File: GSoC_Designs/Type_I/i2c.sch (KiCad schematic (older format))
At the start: 3 parts, among them U5 24AA014, U6 TCA9617A, U7 TCA9617A

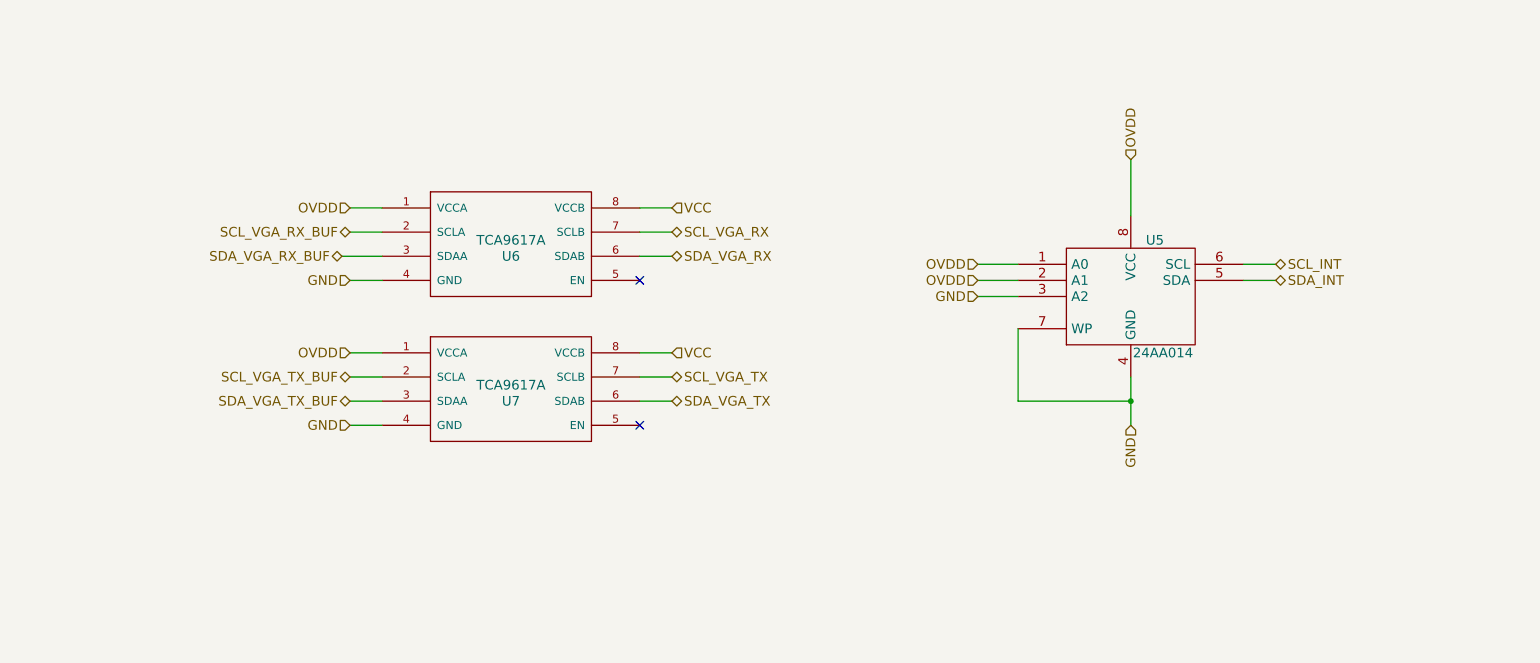
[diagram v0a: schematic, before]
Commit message: Added header for unused Pins
Unused pins are OE_Field, COAST, CLAMP and PWRDWN
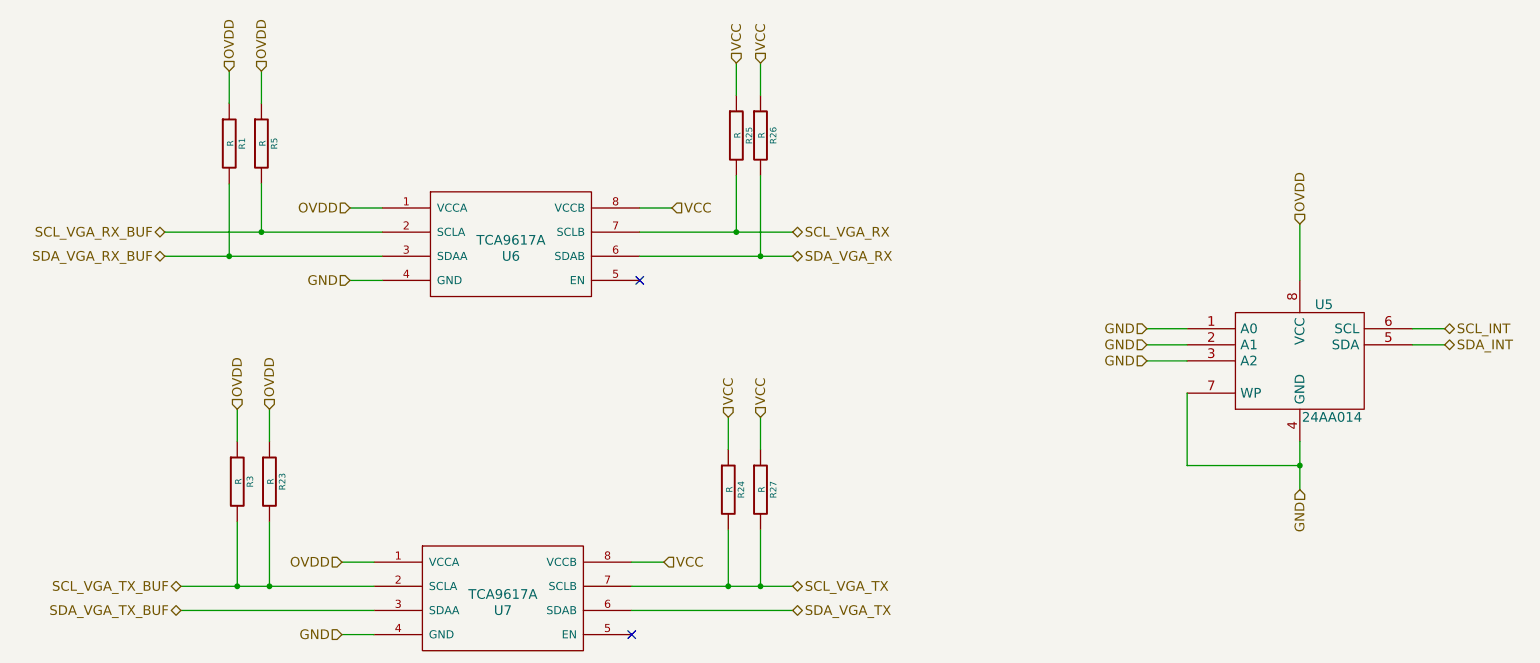
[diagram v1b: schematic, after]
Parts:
- added R1, R23, R24, R25, R26, R27, R3, R5: R, ~, symbol R
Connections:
- net GND: now also U5.1 (A0), U5.2 (A1)
- net OVDD: now also R1.1, R23.1, R3.1, R5.1; no longer U5.1 (A0), U5.2 (A1)
- net SCL_VGA_RX: now also R25.2
- net SCL_VGA_RX_BUF: now also R5.2
- net SCL_VGA_TX: now also R24.2, R27.2
- net SCL_VGA_TX_BUF: now also R23.2, R3.2
- net SDA_VGA_RX: now also R26.2
- net SDA_VGA_RX_BUF: now also R1.2
- net VCC: now also R24.1, R25.1, R26.1, R27.1
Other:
- moved on the sheet: U5, U7

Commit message: PCB Routing
70% tracks routed. Fine tuning remaining
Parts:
- R1, R23, R3, R5: value R -> 2.2K
- R24, R25, R26, R27: value R -> 4.7K
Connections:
- net SCL_VGA_TX: no longer R27.2
- net SCL_VGA_TX_BUF: no longer R3.2
- net SDA_VGA_TX: now also R27.2
- net SDA_VGA_TX_BUF: now also R3.2
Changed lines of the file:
@@
 Sheet 3 3
 Title ""
-Date "17 jul 2014"
+Date "21 jul 2014"
 Rev ""
 Comp ""
@@
 Text HLabel 10000 4150 2    60   BiDi ~ 0
 SDA_INT
-Text HLabel 5150 5500 2    60   Input ~ 0
+Text HLabel 5050 5500 2    60   Input ~ 0
 VCC
 Text HLabel 9100 3400 1    60   Input ~ 0
@@
 	1    0    0    -1
 $EndComp
-Text HLabel 3200 3300 0    60   Input ~ 0
-OVDD
-Text HLabel 3150 5500 0    60   Input ~ 0
-OVDD
-Text HLabel 3150 5950 0    60   Input ~ 0
-GND
-Text HLabel 3200 3750 0    60   Input ~ 0
+Text HLabel 3300 3300 0    60   Input ~ 0
+OVDD
+Text HLabel 3250 5500 0    60   Input ~ 0
+OVDD
+Text HLabel 3250 5950 0    60   Input ~ 0
+GND
+Text HLabel 3300 3750 0    60   Input ~ 0
 GND
 NoConn ~ 4950 5950
 NoConn ~ 5000 3750
-Wire Wire Line
-	9800 4050 10000 4050
-Wire Wire Line
-	9800 4150 10000 4150
-Wire Wire Line
-	9100 3400 9100 3750
-Wire Wire Line
-	9100 4750 9100 4900
-Wire Wire Line
-	9100 4900 9100 5050
-Wire Wire Line
-	8400 4450 8400 4900
-Wire Wire Line
-	8400 4900 9100 4900
-Connection ~ 9100 4900
-Wire Wire Line
-	3200 3300 3400 3300
-Wire Wire Line
-	2050 3450 2650 3450
-Wire Wire Line
-	2650 3450 3400 3450
-Wire Wire Line
-	3200 3750 3400 3750
-Wire Wire Line
-	3150 5500 3350 5500
-Wire Wire Line
-	2150 5650 2500 5650
-Wire Wire Line
-	2500 5650 2700 5650
-Wire Wire Line
-	2700 5650 3350 5650
-Wire Wire Line
-	2150 5800 3350 5800
-Wire Wire Line
-	3150 5950 3350 5950
-Wire Wire Line
-	5000 3450 5600 3450
-Wire Wire Line
-	5600 3450 5950 3450
-Wire Wire Line
-	5000 3600 5750 3600
-Wire Wire Line
-	5750 3600 5950 3600
-Wire Wire Line
-	4950 5500 5150 5500
-Wire Wire Line
-	4950 5650 5550 5650
-Wire Wire Line
-	5550 5650 5750 5650
-Wire Wire Line
-	5750 5650 5950 5650
-Wire Wire Line
-	4950 5800 5950 5800
-Text HLabel 5200 3300 2    60   Input ~ 0
-VCC
-Wire Wire Line
-	5200 3300 5000 3300
+Text HLabel 5100 3300 2    60   Input ~ 0
+VCC
 Text HLabel 8150 4250 0    60   Input ~ 0
 GND
-Wire Wire Line
-	8150 4050 8400 4050
-Wire Wire Line
-	8150 4150 8400 4150
-Wire Wire Line
-	8150 4250 8400 4250
-Wire Wire Line
-	2050 3600 2450 3600
-Wire Wire Line
-	2450 3600 3400 3600
 $Comp
 L R R5
@@
 P 2650 2900
 F 0 "R5" V 2730 2900 40  0000 C CNN
-F 1 "R" V 2657 2901 40  0000 C CNN
+F 1 "2.2K" V 2657 2901 40  0000 C CNN
 F 2 "~" V 2580 2900 30  0000 C CNN
 F 3 "~" H 2650 2900 30  0000 C CNN
@@
 P 2450 2900
 F 0 "R1" V 2530 2900 40  0000 C CNN
-F 1 "R" V 2457 2901 40  0000 C CNN
+F 1 "2.2K" V 2457 2901 40  0000 C CNN
 F 2 "~" V 2380 2900 30  0000 C CNN
 F 3 "~" H 2450 2900 30  0000 C CNN
@@
 P 5600 2850
 F 0 "R25" V 5680 2850 40  0000 C CNN
-F 1 "R" V 5607 2851 40  0000 C CNN
+F 1 "4.7K" V 5607 2851 40  0000 C CNN
 F 2 "~" V 5530 2850 30  0000 C CNN
 F 3 "~" H 5600 2850 30  0000 C CNN
@@
 P 5750 2850
 F 0 "R26" V 5830 2850 40  0000 C CNN
-F 1 "R" V 5757 2851 40  0000 C CNN
+F 1 "4.7K" V 5757 2851 40  0000 C CNN
 F 2 "~" V 5680 2850 30  0000 C CNN
 F 3 "~" H 5750 2850 30  0000 C CNN
@@
 P 2500 5000
 F 0 "R3" V 2580 5000 40  0000 C CNN
-F 1 "R" V 2507 5001 40  0000 C CNN
+F 1 "2.2K" V 2507 5001 40  0000 C CNN
 F 2 "~" V 2430 5000 30  0000 C CNN
 F 3 "~" H 2500 5000 30  0000 C CNN
@@
 P 2700 5000
 F 0 "R23" V 2780 5000 40  0000 C CNN
-F 1 "R" V 2707 5001 40  0000 C CNN
+F 1 "2.2K" V 2707 5001 40  0000 C CNN
 F 2 "~" V 2630 5000 30  0000 C CNN
 F 3 "~" H 2700 5000 30  0000 C CNN
@@
 P 5550 5050
 F 0 "R24" V 5630 5050 40  0000 C CNN
-F 1 "R" V 5557 5051 40  0000 C CNN
+F 1 "4.7K" V 5557 5051 40  0000 C CNN
 F 2 "~" V 5480 5050 30  0000 C CNN
 F 3 "~" H 5550 5050 30  0000 C CNN
@@
 P 5750 5050
 F 0 "R27" V 5830 5050 40  0000 C CNN
-F 1 "R" V 5757 5051 40  0000 C CNN
+F 1 "4.7K" V 5757 5051 40  0000 C CNN
 F 2 "~" V 5680 5050 30  0000 C CNN
 F 3 "~" H 5750 5050 30  0000 C CNN
@@
 	1    0    0    -1
 $EndComp
+Text HLabel 2650 2450 1    60   Input ~ 0
+OVDD
+Text HLabel 2450 2450 1    60   Input ~ 0
+OVDD
+Text HLabel 5600 2400 1    60   Input ~ 0
+VCC
+Text HLabel 5750 2400 1    60   Input ~ 0
+VCC
+Text HLabel 2700 4550 1    60   Input ~ 0
+OVDD
+Text HLabel 2500 4550 1    60   Input ~ 0
+OVDD
+Text HLabel 5550 4600 1    60   Input ~ 0
+VCC
+Text HLabel 5750 4600 1    60   Input ~ 0
+VCC
+Text HLabel 8150 4150 0    60   Input ~ 0
+GND
+Text HLabel 8150 4050 0    60   Input ~ 0
+GND
+Wire Wire Line
+	9800 4050 10000 4050
+Wire Wire Line
+	9800 4150 10000 4150
+Wire Wire Line
+	9100 3400 9100 3750
+Wire Wire Line
+	9100 4750 9100 5050
+Wire Wire Line
+	8400 4450 8400 4900
+Wire Wire Line
+	8400 4900 9100 4900
+Connection ~ 9100 4900
+Wire Wire Line
+	3300 3300 3400 3300
+Wire Wire Line
+	2050 3450 3400 3450
+Wire Wire Line
+	3300 3750 3400 3750
+Wire Wire Line
+	3250 5500 3350 5500
+Wire Wire Line
+	2150 5650 3350 5650
+Wire Wire Line
+	2150 5800 3350 5800
+Wire Wire Line
+	3250 5950 3350 5950
+Wire Wire Line
+	5000 3450 5950 3450
+Wire Wire Line
+	5000 3600 5950 3600
+Wire Wire Line
+	4950 5500 5050 5500
+Wire Wire Line
+	4950 5650 5950 5650
+Wire Wire Line
+	4950 5800 5950 5800
+Wire Wire Line
+	5100 3300 5000 3300
+Wire Wire Line
+	8150 4050 8400 4050
+Wire Wire Line
+	8150 4150 8400 4150
+Wire Wire Line
+	8150 4250 8400 4250
+Wire Wire Line
+	2050 3600 3400 3600
 Wire Wire Line
 	2650 3150 2650 3450
 Connection ~ 2650 3450
-Text HLabel 2650 2450 1    60   Input ~ 0
-OVDD
-Text HLabel 2450 2450 1    60   Input ~ 0
-OVDD
 Wire Wire Line
 	2450 2450 2450 2650
@@
 	5750 3100 5750 3600
 Connection ~ 5750 3600
-Text HLabel 5600 2400 1    60   Input ~ 0
-VCC
-Text HLabel 5750 2400 1    60   Input ~ 0
-VCC
 Wire Wire Line
 	5600 2600 5600 2400
 Wire Wire Line
 	5750 2600 5750 2400
-Text HLabel 2700 4550 1    60   Input ~ 0
-OVDD
-Text HLabel 2500 4550 1    60   Input ~ 0
-OVDD
-Text HLabel 5550 4600 1    60   Input ~ 0
-VCC
-Text HLabel 5750 4600 1    60   Input ~ 0
-VCC
-Wire Wire Line
-	2500 5250 2500 5650
-Connection ~ 2500 5650
 Wire Wire Line
 	2700 5250 2700 5650
@@
 Connection ~ 5550 5650
 Wire Wire Line
-	5750 5300 5750 5650
-Connection ~ 5750 5650
-Wire Wire Line
 	5550 4600 5550 4800
 Wire Wire Line
 	5750 4600 5750 4800
-Text HLabel 8150 4150 0    60   Input ~ 0
-GND
-Text HLabel 8150 4050 0    60   Input ~ 0
-GND
+Wire Wire Line
+	2500 5250 2500 5800
+Connection ~ 2500 5800
+Wire Wire Line
+	5750 5300 5750 5800
+Connection ~ 5750 5800
 $EndSCHEMATC
